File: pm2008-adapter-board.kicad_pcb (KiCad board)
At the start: 2 copper layers, 14 x 20 mm, 3 parts, among them J1 Conn_02x05_Top_Bottom, J2 Conn_01x04, J3 Conn_01x02

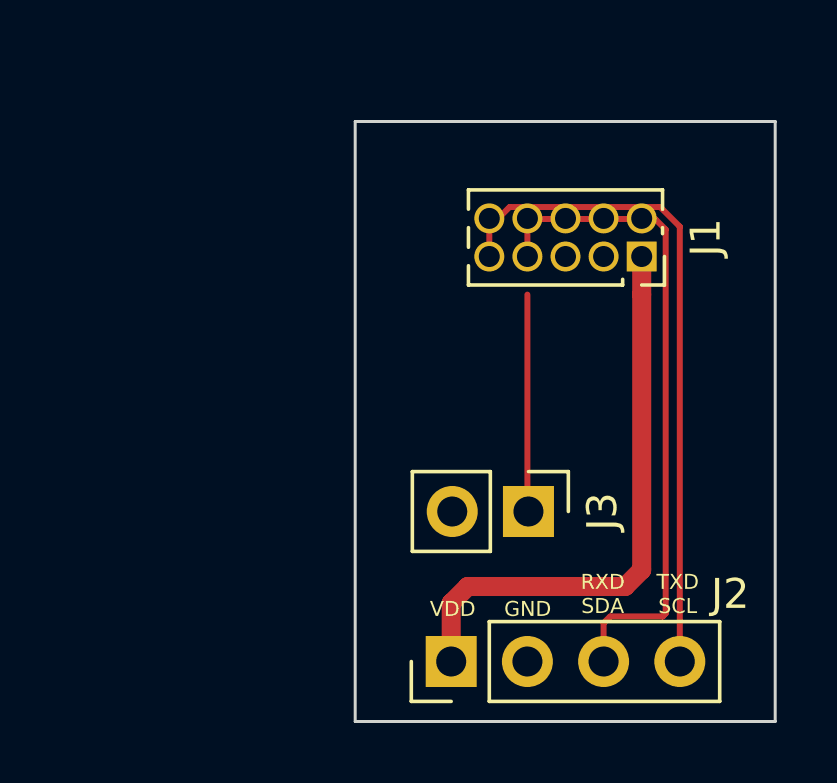
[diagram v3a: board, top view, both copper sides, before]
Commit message: feat: update artwork
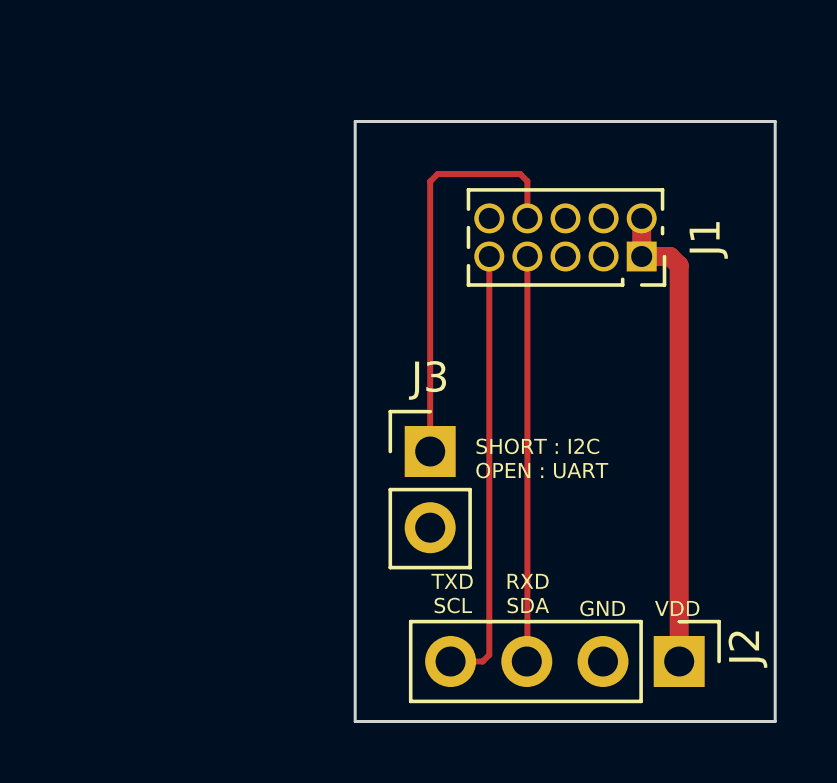
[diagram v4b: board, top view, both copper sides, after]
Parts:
- moved J2 7.60 mm to (150.8, 108.0), turned to -90 degrees
- moved J3 3.84 mm to (142.5, 101.0), turned to 0 degrees
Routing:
- net /TXD/SCL: track 44.5 -> 14.7 mm
- net /RXD/SDA: track 0.00 -> 13.5 mm
- net /CTL: track 7.24 -> 13.7 mm
- net VDD: track 19.2 -> 15.8 mm
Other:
- board text added: "SHORT : I2C OPEN : UART"
- board text added: "V01"
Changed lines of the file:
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@@
     )
     (pad_to_mask_clearance 0)
-    (grid_origin 140 90)
     (pcbplotparams
       (layerselection 0x00010fc_ffffffff)
@@
       (outputformat 1)
       (mirror false)
-      (drillshape 1)
+      (drillshape 0)
       (scaleselection 1)
-      (outputdirectory "")
+      (outputdirectory "gerber/")
     )
   )
@@
       (effects (font (size 1 1) (thickness 0.15)))
     )
-    (fp_text value "Conn_02x05_Top_Bottom" (at -0.635 7.215 -90) (layer "F.Fab")
+    (fp_text value "Conn_02x05_Top_Bottom" (at -0.635 7.215 -90) (layer "F.Fab") hide
       (effects (font (size 1 1) (thickness 0.15)))
     )
@@
   )
   (footprint "Connector_PinHeader_2.54mm:PinHeader_1x02_P2.54mm_Vertical" (layer "F.Cu")
-    (at 145.775 103 -90)
+    (at 142.5 101)
     (descr "Through hole straight pin header, 1x02, 2.54mm pitch, single row")
     (tags "Through hole pin header THT 1x02 2.54mm single row")
@@
     (property "Sheetname" "")
     (attr through_hole)
-    (fp_text reference "J3" (at 0 -2.46 90) (layer "F.SilkS")
-      (effects (font (size 1 1) (thickness 0.15)))
-    )
-    (fp_text value "Conn_01x02" (at 0 4.87 90) (layer "F.Fab") hide
-      (effects (font (size 1 1) (thickness 0.15)))
-    )
-    (fp_text user "${REFERENCE}" (at 0 1.27) (layer "F.Fab")
+    (fp_text reference "J3" (at 0 -2.46) (layer "F.SilkS")
+      (effects (font (size 1 1) (thickness 0.15)))
+    )
+    (fp_text value "Conn_01x02" (at 0 4.87) (layer "F.Fab") hide
+      (effects (font (size 1 1) (thickness 0.15)))
+    )
+    (fp_text user "${REFERENCE}" (at 0 1.27 90) (layer "F.Fab")
       (effects (font (size 1 1) (thickness 0.15)))
     )
@@
     (fp_line (start 1.27 -1.27) (end 1.27 3.81) (layer "F.Fab") (width 0.1))
     (fp_line (start -1.27 -0.635) (end -0.635 -1.27) (layer "F.Fab") (width 0.1))
-    (pad "1" thru_hole rect (at 0 0 270) (size 1.7 1.7) (drill 1) (layers *.Cu *.Mask)
+    (pad "1" thru_hole rect (at 0 0) (size 1.7 1.7) (drill 1) (layers *.Cu *.Mask)
       (net 6 "/CTL") (pinfunction "Pin_1") (pintype "passive"))
-    (pad "2" thru_hole oval (at 0 2.54 270) (size 1.7 1.7) (drill 1) (layers *.Cu *.Mask)
+    (pad "2" thru_hole oval (at 0 2.54) (size 1.7 1.7) (drill 1) (layers *.Cu *.Mask)
       (net 2 "Earth") (pinfunction "Pin_2") (pintype "passive"))
     (model "${KICAD6_3DMODEL_DIR}/Connector_PinHeader_2.54mm.3dshapes/PinHeader_1x02_P2.54mm_Vertical.wrl"
@@
   )
   (footprint "Connector_PinHeader_2.54mm:PinHeader_1x04_P2.54mm_Vertical" (layer "F.Cu")
-    (at 143.2 108 90)
+    (at 150.8 108 -90)
     (descr "Through hole straight pin header, 1x04, 2.54mm pitch, single row")
     (tags "Through hole pin header THT 1x04 2.54mm single row")
@@
     (property "Sheetname" "")
     (attr through_hole)
-    (fp_text reference "J2" (at 2.25 9.3 180) (layer "F.SilkS")
+    (fp_text reference "J2" (at -0.5 -2.2 90) (layer "F.SilkS")
       (effects (font (size 1 1) (thickness 0.15)))
     )
@@
     (fp_line (start 1.27 8.89) (end -1.27 8.89) (layer "F.Fab") (width 0.1))
     (fp_line (start -0.635 -1.27) (end 1.27 -1.27) (layer "F.Fab") (width 0.1))
-    (pad "1" thru_hole rect (at 0 0 90) (size 1.7 1.7) (drill 1) (layers *.Cu *.Mask)
+    (pad "1" thru_hole rect (at 0 0 270) (size 1.7 1.7) (drill 1) (layers *.Cu *.Mask)
       (net 1 "VDD") (pinfunction "Pin_1") (pintype "passive"))
-    (pad "2" thru_hole oval (at 0 2.54 90) (size 1.7 1.7) (drill 1) (layers *.Cu *.Mask)
+    (pad "2" thru_hole oval (at 0 2.54 270) (size 1.7 1.7) (drill 1) (layers *.Cu *.Mask)
       (net 2 "Earth") (pinfunction "Pin_2") (pintype "passive"))
-    (pad "3" thru_hole oval (at 0 5.08 90) (size 1.7 1.7) (drill 1) (layers *.Cu *.Mask)
+    (pad "3" thru_hole oval (at 0 5.08 270) (size 1.7 1.7) (drill 1) (layers *.Cu *.Mask)
       (net 5 "/RXD{slash}SDA") (pinfunction "Pin_3") (pintype "passive"))
-    (pad "4" thru_hole oval (at 0 7.62 90) (size 1.7 1.7) (drill 1) (layers *.Cu *.Mask)
+    (pad "4" thru_hole oval (at 0 7.62 270) (size 1.7 1.7) (drill 1) (layers *.Cu *.Mask)
       (net 7 "/TXD{slash}SCL") (pinfunction "Pin_4") (pintype "passive"))
     (model "${KICAD6_3DMODEL_DIR}/Connector_PinHeader_2.54mm.3dshapes/PinHeader_1x04_P2.54mm_Vertical.wrl"
@@
   (gr_line (start 140 90) (end 154 90) (layer "Edge.Cuts") (width 0.1))
   (gr_line (start 154 90) (end 154 110) (layer "Edge.Cuts") (width 0.1))
-  (gr_text "RXD\nSDA" (at 148.25 105.75) (layer "F.SilkS")
-    (effects (font (size 0.5 0.5) (thickness 0.075)))
-  )
-  (gr_text "VDD" (at 143.25 106.25) (layer "F.SilkS")
-    (effects (font (size 0.5 0.5) (thickness 0.075)))
-  )
-  (gr_text "TXD\nSCL" (at 150.75 105.75) (layer "F.SilkS")
-    (effects (font (size 0.5 0.5) (thickness 0.075)))
-  )
-  (gr_text "GND" (at 145.75 106.25) (layer "F.SilkS")
-    (effects (font (size 0.5 0.5) (thickness 0.075)))
-  )
-  (segment (start 149 105.5) (end 149.55 104.95) (width 0.635) (layer "F.Cu") (net 1))
-  (segment (start 149.55 104.95) (end 149.55 95.77) (width 0.635) (layer "F.Cu") (net 1))
-  (segment (start 143.2 108) (end 143.2 106.05) (width 0.635) (layer "F.Cu") (net 1))
-  (segment (start 149.55 95.77) (end 149.55 94.5) (width 0.635) (layer "F.Cu") (net 1))
-  (segment (start 143.75 105.5) (end 149 105.5) (width 0.635) (layer "F.Cu") (net 1))
-  (segment (start 143.2 106.05) (end 143.75 105.5) (width 0.635) (layer "F.Cu") (net 1))
-  (segment (start 145.74 95.77) (end 145.74 102.965) (width 0.2) (layer "F.Cu") (net 6))
-  (segment (start 145.74 102.965) (end 145.775 103) (width 0.2) (layer "F.Cu") (net 6))
-  (segment (start 144.47 93.53) (end 145.149519 92.850481) (width 0.2) (layer "F.Cu") (net 7))
-  (segment (start 145.74 93.51) (end 146 93.25) (width 0.2) (layer "F.Cu") (net 7))
-  (segment (start 150.25 106.5) (end 148.5 106.5) (width 0.2) (layer "F.Cu") (net 7))
-  (segment (start 150.165487 92.850481) (end 150.82 93.504994) (width 0.2) (layer "F.Cu") (net 7))
-  (segment (start 148.5 106.5) (end 148.28 106.72) (width 0.2) (layer "F.Cu") (net 7))
-  (segment (start 144.47 94.5) (end 144.47 93.53) (width 0.2) (layer "F.Cu") (net 7))
-  (segment (start 146 93.25) (end 150 93.25) (width 0.2) (layer "F.Cu") (net 7))
-  (segment (start 145.74 94.5) (end 145.74 93.51) (width 0.2) (layer "F.Cu") (net 7))
-  (segment (start 150.349511 93.599511) (end 150.349511 106.400489) (width 0.2) (layer "F.Cu") (net 7))
-  (segment (start 150 93.25) (end 150.349511 93.599511) (width 0.2) (layer "F.Cu") (net 7))
-  (segment (start 145.149519 92.850481) (end 150.165487 92.850481) (width 0.2) (layer "F.Cu") (net 7))
-  (segment (start 150.82 93.504994) (end 150.82 108) (width 0.2) (layer "F.Cu") (net 7))
-  (segment (start 150.349511 106.400489) (end 150.25 106.5) (width 0.2) (layer "F.Cu") (net 7))
-  (segment (start 148.28 106.72) (end 148.28 108) (width 0.2) (layer "F.Cu") (net 7))
+  (gr_text "V01" (at 152.25 91) (layer "B.SilkS")
+    (effects (font (size 1 1) (thickness 0.15)) (justify mirror))
+  )
+  (gr_text "SHORT : I2C\nOPEN : UART" (at 144 101.25) (layer "F.SilkS")
+    (effects (font (size 0.5 0.5) (thickness 0.075)) (justify left))
+  )
+  (gr_text "RXD\nSDA" (at 145.75 105.75) (layer "F.SilkS")
+    (effects (font (size 0.5 0.5) (thickness 0.075)))
+  )
+  (gr_text "VDD" (at 150.75 106.25) (layer "F.SilkS")
+    (effects (font (size 0.5 0.5) (thickness 0.075)))
+  )
+  (gr_text "TXD\nSCL" (at 143.25 105.75) (layer "F.SilkS")
+    (effects (font (size 0.5 0.5) (thickness 0.075)))
+  )
+  (gr_text "GND" (at 148.25 106.25) (layer "F.SilkS")
+    (effects (font (size 0.5 0.5) (thickness 0.075)))
+  )
+  (segment (start 149.55 94.5) (end 149.55 93.23) (width 0.635) (layer "F.Cu") (net 1))
+  (segment (start 150.5 94.5) (end 149.55 94.5) (width 0.635) (layer "F.Cu") (net 1))
+  (segment (start 150.8 108) (end 150.8 94.8) (width 0.635) (layer "F.Cu") (net 1))
+  (segment (start 150.8 94.8) (end 150.5 94.5) (width 0.635) (layer "F.Cu") (net 1))
+  (segment (start 145.74 94.5) (end 145.74 107.98) (width 0.2) (layer "F.Cu") (net 5))
+  (segment (start 145.74 107.98) (end 145.72 108) (width 0.2) (layer "F.Cu") (net 5))
+  (segment (start 145.74 91.99) (end 145.5 91.75) (width 0.2) (layer "F.Cu") (net 6))
+  (segment (start 142.5 92) (end 142.5 101) (width 0.2) (layer "F.Cu") (net 6))
+  (segment (start 145.5 91.75) (end 142.75 91.75) (width 0.2) (layer "F.Cu") (net 6))
+  (segment (start 142.75 91.75) (end 142.5 92) (width 0.2) (layer "F.Cu") (net 6))
+  (segment (start 145.74 93.23) (end 145.74 91.99) (width 0.2) (layer "F.Cu") (net 6))
+  (segment (start 144.47 107.78) (end 144.25 108) (width 0.2) (layer "F.Cu") (net 7))
+  (segment (start 144.25 108) (end 143.18 108) (width 0.2) (layer "F.Cu") (net 7))
+  (segment (start 144.47 94.5) (end 144.47 107.78) (width 0.2) (layer "F.Cu") (net 7))
   (zone (net 2) (net_name "Earth") (layers F&B.Cu) (hatch edge 0.508)
     (connect_pads (clearance 0.508))
     (min_thickness 0.254) (filled_areas_thickness no)
-    (fill (thermal_gap 0.508) (thermal_bridge_width 0.508))
+    (fill yes (thermal_gap 0.508) (thermal_bridge_width 0.508))
     (polygon
       (pts

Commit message: feat: update artwork
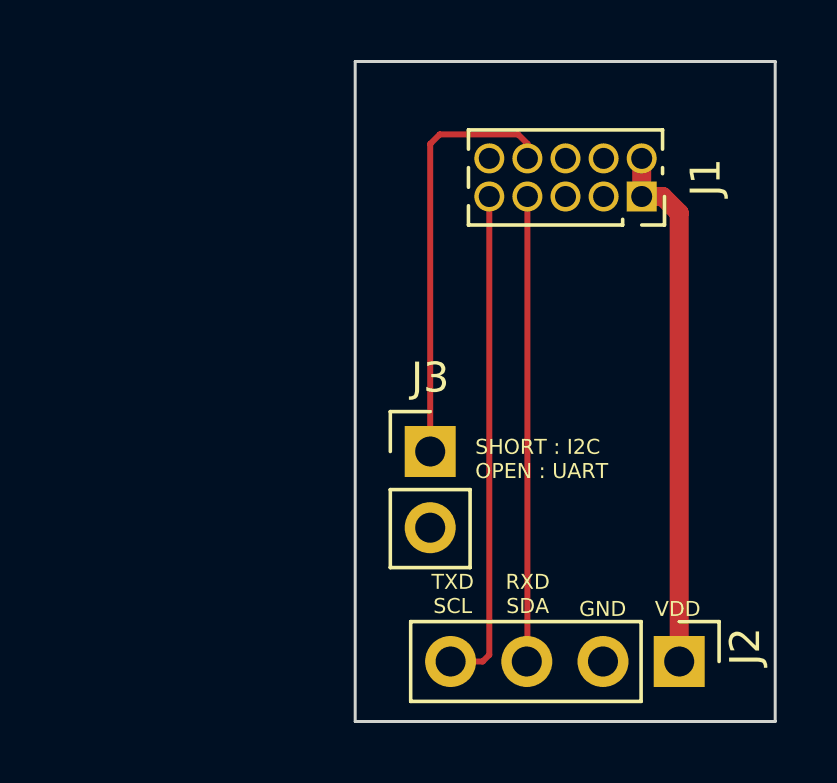
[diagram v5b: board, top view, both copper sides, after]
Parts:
- moved J1 2.00 mm to (149.6, 92.5)
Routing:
- net /TXD/SCL: track 14.7 -> 16.7 mm
- net /RXD/SDA: track 13.5 -> 15.5 mm
- net VDD: track 15.8 -> 17.7 mm
- net /CTL: track 13.7 -> 14.2 mm
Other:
- board size 14 x 20 mm -> 14 x 22 mm
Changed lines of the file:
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@@
   (net 8 "unconnected-(J1-Pad10)")
   (footprint "Connector_PinSocket_1.27mm:PinSocket_2x05_P1.27mm_Vertical" (layer "F.Cu")
-    (at 149.55 94.5 -90)
+    (at 149.55 92.5 -90)
     (descr "Through hole straight socket strip, 2x05, 1.27mm pitch, double cols (from Kicad 4.0.7), script generated")
     (tags "Through hole socket strip THT 2x05 1.27mm double row")
@@
   )
   (gr_line (start 140 110) (end 154 110) (layer "Edge.Cuts") (width 0.1))
-  (gr_line (start 140 110) (end 140 90) (layer "Edge.Cuts") (width 0.1))
-  (gr_line (start 140 90) (end 154 90) (layer "Edge.Cuts") (width 0.1))
-  (gr_line (start 154 90) (end 154 110) (layer "Edge.Cuts") (width 0.1))
-  (gr_text "V01" (at 152.25 91) (layer "B.SilkS")
+  (gr_line (start 140 110) (end 140 88) (layer "Edge.Cuts") (width 0.1))
+  (gr_line (start 140 88) (end 154 88) (layer "Edge.Cuts") (width 0.1))
+  (gr_line (start 154 88) (end 154 110) (layer "Edge.Cuts") (width 0.1))
+  (gr_text "V01" (at 152.25 89) (layer "B.SilkS")
     (effects (font (size 1 1) (thickness 0.15)) (justify mirror))
   )
@@
     (effects (font (size 0.5 0.5) (thickness 0.075)))
   )
-  (segment (start 149.55 94.5) (end 149.55 93.23) (width 0.635) (layer "F.Cu") (net 1))
-  (segment (start 150.5 94.5) (end 149.55 94.5) (width 0.635) (layer "F.Cu") (net 1))
-  (segment (start 150.8 108) (end 150.8 94.8) (width 0.635) (layer "F.Cu") (net 1))
-  (segment (start 150.8 94.8) (end 150.5 94.5) (width 0.635) (layer "F.Cu") (net 1))
-  (segment (start 145.74 94.5) (end 145.74 107.98) (width 0.2) (layer "F.Cu") (net 5))
+  (segment (start 150.8 108) (end 150.8 93.05) (width 0.635) (layer "F.Cu") (net 1))
+  (segment (start 150.8 93.05) (end 150.25 92.5) (width 0.635) (layer "F.Cu") (net 1))
+  (segment (start 149.55 92.5) (end 149.55 91.23) (width 0.635) (layer "F.Cu") (net 1))
+  (segment (start 150.25 92.5) (end 149.55 92.5) (width 0.635) (layer "F.Cu") (net 1))
+  (segment (start 145.74 92.5) (end 145.74 107.98) (width 0.2) (layer "F.Cu") (net 5))
   (segment (start 145.74 107.98) (end 145.72 108) (width 0.2) (layer "F.Cu") (net 5))
-  (segment (start 145.74 91.99) (end 145.5 91.75) (width 0.2) (layer "F.Cu") (net 6))
-  (segment (start 142.5 92) (end 142.5 101) (width 0.2) (layer "F.Cu") (net 6))
-  (segment (start 145.5 91.75) (end 142.75 91.75) (width 0.2) (layer "F.Cu") (net 6))
-  (segment (start 142.75 91.75) (end 142.5 92) (width 0.2) (layer "F.Cu") (net 6))
-  (segment (start 145.74 93.23) (end 145.74 91.99) (width 0.2) (layer "F.Cu") (net 6))
+  (segment (start 145.430489 90.430489) (end 145.75 90.75) (width 0.2) (layer "F.Cu") (net 6))
+  (segment (start 142.5 90.75) (end 142.819511 90.430489) (width 0.2) (layer "F.Cu") (net 6))
+  (segment (start 142.819511 90.430489) (end 145.430489 90.430489) (width 0.2) (layer "F.Cu") (net 6))
+  (segment (start 142.5 101) (end 142.5 90.75) (width 0.2) (layer "F.Cu") (net 6))
+  (segment (start 145.75 90.75) (end 145.75 91.22) (width 0.2) (layer "F.Cu") (net 6))
+  (segment (start 145.75 91.22) (end 145.74 91.23) (width 0.2) (layer "F.Cu") (net 6))
+  (segment (start 144.47 92.5) (end 144.47 107.78) (width 0.2) (layer "F.Cu") (net 7))
   (segment (start 144.47 107.78) (end 144.25 108) (width 0.2) (layer "F.Cu") (net 7))
   (segment (start 144.25 108) (end 143.18 108) (width 0.2) (layer "F.Cu") (net 7))
-  (segment (start 144.47 94.5) (end 144.47 107.78) (width 0.2) (layer "F.Cu") (net 7))
   (zone (net 2) (net_name "Earth") (layers F&B.Cu) (hatch edge 0.508)
     (connect_pads (clearance 0.508))
@@
         (xy 154 110)
         (xy 140 110)
-        (xy 140 90)
-        (xy 154 90)
+        (xy 140 88)
+        (xy 154 88)
       )
     )
